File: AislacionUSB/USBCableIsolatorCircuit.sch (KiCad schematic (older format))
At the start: 54 parts, among them CON1 BARREL_JACK, J1 MICRO_USB, J2 IN_VCC, P1 USB_A, U1 PRTR5V0U2X, U2 ADUM5000, U3 7805, U4 PRTR5V0U2X

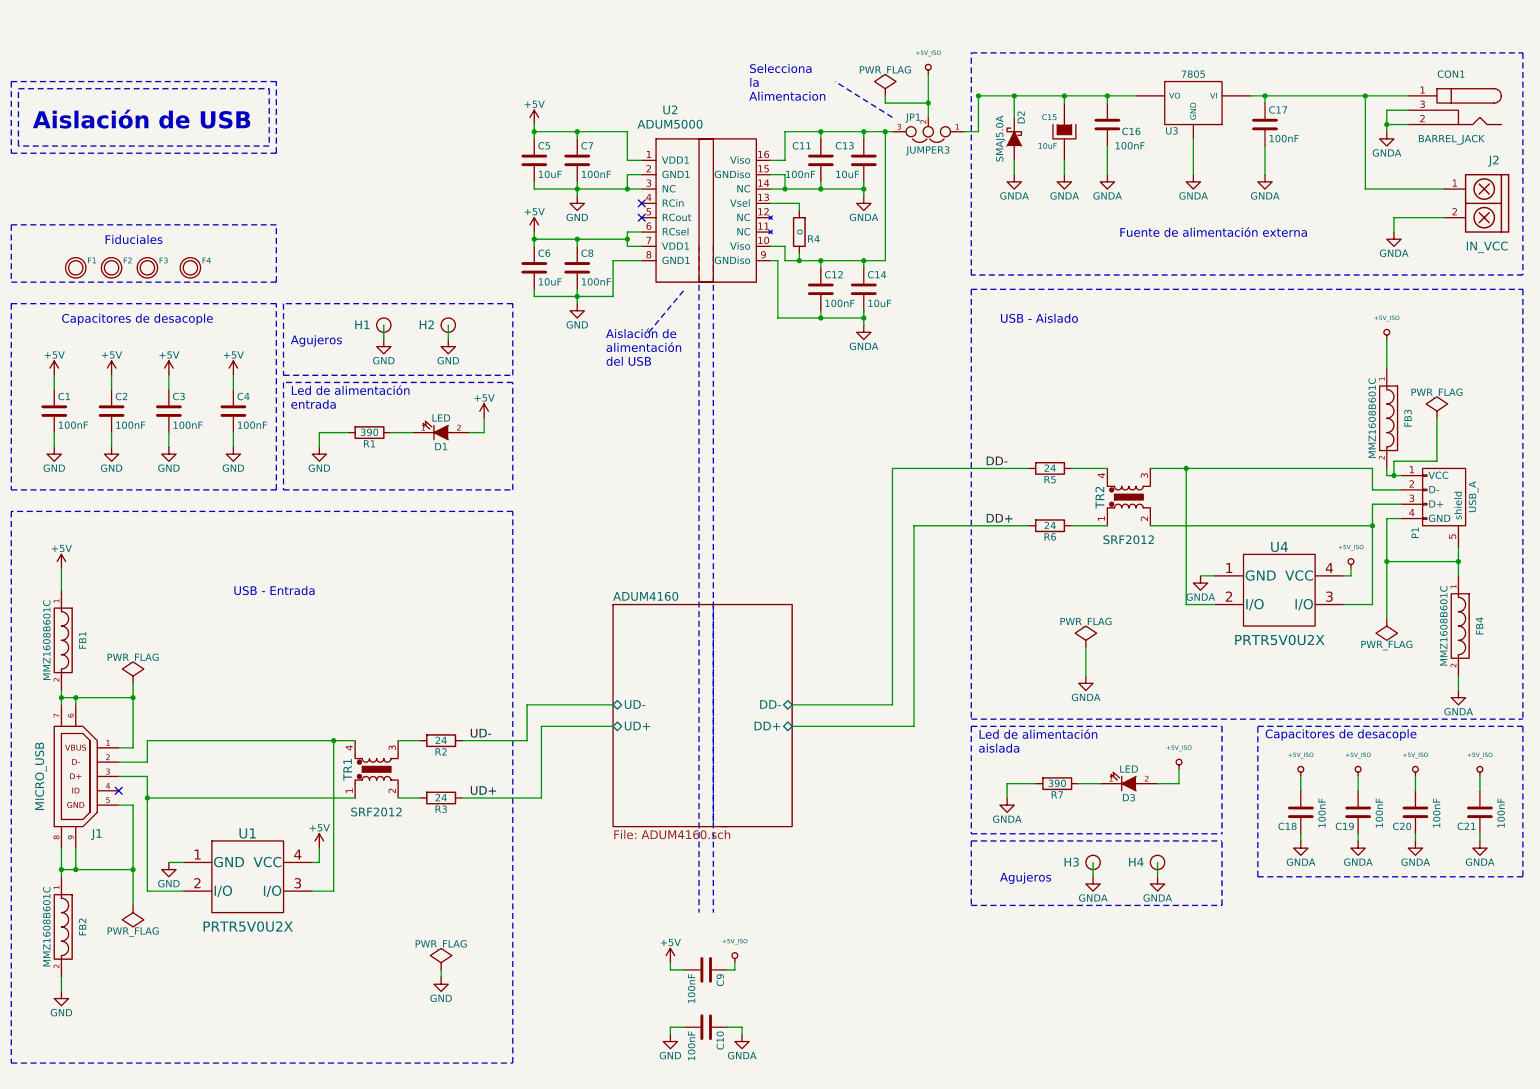
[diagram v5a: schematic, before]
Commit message: Primer ruteo - Se eliminaron los agujeros
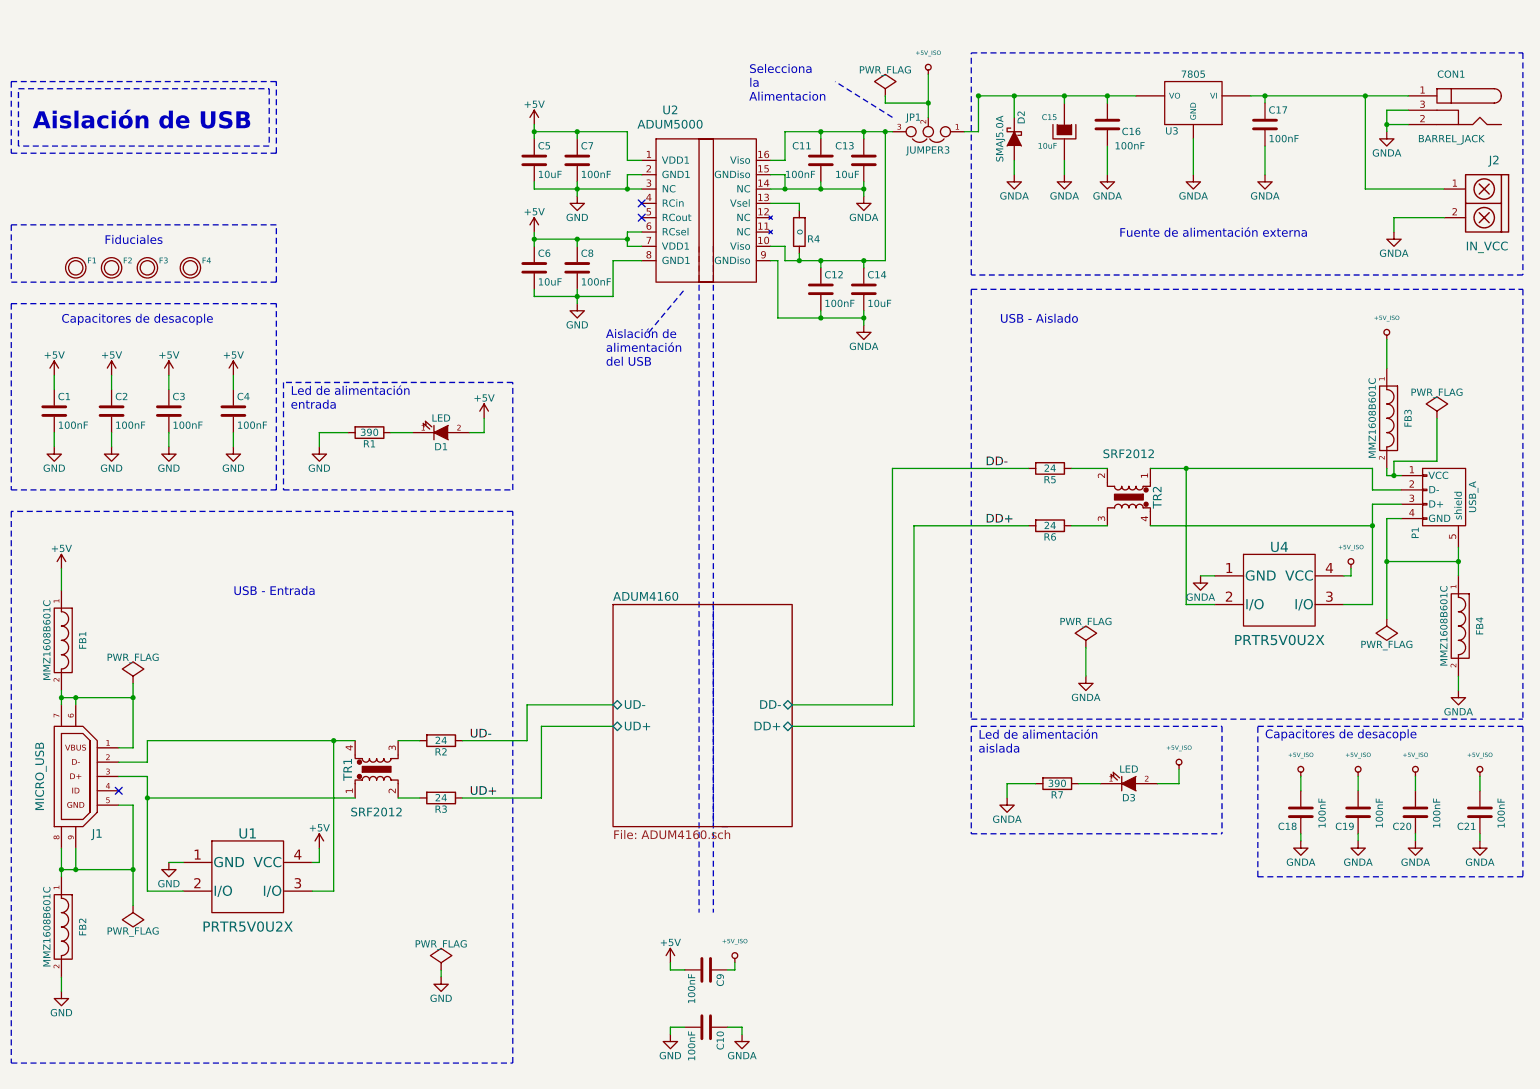
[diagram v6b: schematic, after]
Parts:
- removed H1, H2, H3, H4: PCB_HOLE, Mounting_Holes:MountingHole_2.7mm, symbol PCB_HOLE
- D2: footprint Diodes_SMD:DO-214AB_Handsoldering -> AislacionUSB:DO-214AC_SMA
- F1, F2, F3, F4: footprint Fiducials:Fiducial_1mm_Dia_2.54mm_Outer_CopperBottom -> AislacionUSB:Fiducial_1mm
- U3: Desc Linear Voltage Regulator IC Positive Fixed 1 Output 5V 1A TO-220AB -> Linear Voltage Regulator IC Positive Fixed 1 Output 5V 1A TO-220AB
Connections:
- net at P1.2 (D-), U4.2 (I/O): now also TR2.1; no longer TR2.3
- net at P1.3 (D+), U4.3 (I/O): now also TR2.4; no longer TR2.2
- net at R6.1: now also TR2.3; no longer TR2.1
- net at R5.1: now also TR2.2; no longer TR2.4
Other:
- note removed: "Agujeros"
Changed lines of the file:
@@
 $EndDescr
-$Comp
-L 7805 U3
-U 1 1 577C4B1F
-P 8850 900
-F 0 "U3" H 9000 704 50  0000 C CNN
-F 1 "7805" H 8850 1100 50  0000 C CNN
-F 2 "Power_Integrations:TO-220" H 8850 900 50  0001 C CNN
-F 3 "" H 8850 900 50  0000 C CNN
-F 4 "	Linear Voltage Regulator IC Positive Fixed 1 Output 5V 1A TO-220AB" H 8850 900 60  0001 C CNN "Desc"
-F 5 "LM7805CT-ND" H 8850 900 60  0001 C CNN "Digikey#"
-F 6 "LM7805CT" H 8850 900 60  0001 C CNN "Manf#"
-F 7 "Fairchild Semiconductor" H 8850 900 60  0001 C CNN "Manf"
-	1    8850 900
-	-1   0    0    -1
-$EndComp
 $Comp
 L BARREL_JACK CON1
@@
 F 0 "D2" H 7450 1100 50  0000 C CNN
 F 1 "SMAJ5.0A" H 7600 1250 50  0000 C CNN
-F 2 "Diodes_SMD:DO-214AB_Handsoldering" H 7600 1150 50  0001 C CNN
+F 2 "AislacionUSB:DO-214AC_SMA" H 7600 1150 50  0001 C CNN
 F 3 "" H 7600 1150 50  0000 C CNN
 F 4 "SMAJ5.0ABCT-ND" H 7600 1150 60  0001 C CNN "Digikey#"
@@
 F 0 "F1" H 1130 2100 40  0000 L CNN
 F 1 "FIDUCIAL" H 1050 1950 30  0001 C CNN
-F 2 "Fiducials:Fiducial_1mm_Dia_2.54mm_Outer_CopperBottom" H 1050 2100 60  0001 C CNN
+F 2 "AislacionUSB:Fiducial_1mm" H 1050 2100 60  0001 C CNN
 F 3 "" H 1050 2100 60  0001 C CNN
 F 4 "FIDUCIAL" H 1100 1850 60  0001 C CNN "Descripcion"
@@
 F 0 "F2" H 1380 2100 40  0000 L CNN
 F 1 "FIDUCIAL" H 1300 1950 30  0001 C CNN
-F 2 "Fiducials:Fiducial_1mm_Dia_2.54mm_Outer_CopperBottom" H 1300 2100 60  0001 C CNN
+F 2 "AislacionUSB:Fiducial_1mm" H 1300 2100 60  0001 C CNN
 F 3 "" H 1300 2100 60  0001 C CNN
 F 4 "FIDUCIAL" H 1350 1850 60  0001 C CNN "Descripcion"
@@
 F 0 "F3" H 1630 2100 40  0000 L CNN
 F 1 "FIDUCIAL" H 1550 1950 30  0001 C CNN
-F 2 "Fiducials:Fiducial_1mm_Dia_2.54mm_Outer_CopperBottom" H 1550 2100 60  0001 C CNN
+F 2 "AislacionUSB:Fiducial_1mm" H 1550 2100 60  0001 C CNN
 F 3 "" H 1550 2100 60  0001 C CNN
 F 4 "FIDUCIAL" H 1600 1850 60  0001 C CNN "Descripcion"
@@
 F 0 "F4" H 1930 2100 40  0000 L CNN
 F 1 "FIDUCIAL" H 1850 1950 30  0001 C CNN
-F 2 "Fiducials:Fiducial_1mm_Dia_2.54mm_Outer_CopperBottom" H 1850 2100 60  0001 C CNN
+F 2 "AislacionUSB:Fiducial_1mm" H 1850 2100 60  0001 C CNN
 F 3 "" H 1850 2100 60  0001 C CNN
 F 4 "FIDUCIAL" H 1900 1850 60  0001 C CNN "Descripcion"
@@
 Text Notes 750  1100 0    118  ~ 24
 Aislación de USB\n
-$Comp
-L PCB_HOLE H1
-U 1 1 578E72CD
-P 3200 2450
-F 0 "H1" H 3050 2450 60  0000 C CNN
-F 1 "PCB_HOLE" H 2900 2350 60  0001 C CNN
-F 2 "Mounting_Holes:MountingHole_2.7mm" H 3050 2500 60  0001 C CNN
-F 3 "PCB HOLE" H 3150 2600 60  0001 C CNN
-	1    3200 2450
-	1    0    0    -1
-$EndComp
-$Comp
-L PCB_HOLE H2
-U 1 1 578E7442
-P 3650 2450
-F 0 "H2" H 3500 2450 60  0000 C CNN
-F 1 "PCB_HOLE" H 3350 2350 60  0001 C CNN
-F 2 "Mounting_Holes:MountingHole_2.7mm" H 3500 2500 60  0001 C CNN
-F 3 "PCB HOLE" H 3600 2600 60  0001 C CNN
-	1    3650 2450
-	1    0    0    -1
-$EndComp
-$Comp
-L GND #PWR046
-U 1 1 578E8B5D
-P 3200 2550
-F 0 "#PWR046" H 3200 2300 50  0001 C CNN
-F 1 "GND" H 3200 2400 50  0000 C CNN
-F 2 "" H 3200 2550 50  0000 C CNN
-F 3 "" H 3200 2550 50  0000 C CNN
-	1    3200 2550
-	1    0    0    -1
-$EndComp
-$Comp
-L GND #PWR047
-U 1 1 578E8EB5
-P 3650 2550
-F 0 "#PWR047" H 3650 2300 50  0001 C CNN
-F 1 "GND" H 3650 2400 50  0000 C CNN
-F 2 "" H 3650 2550 50  0000 C CNN
-F 3 "" H 3650 2550 50  0000 C CNN
-	1    3650 2550
-	1    0    0    -1
-$EndComp
 Wire Wire Line
 	1450 5400 1350 5400
@@
 Wire Notes Line
 	600  1750 600  2150
-Wire Wire Line
-	3200 2450 3200 2550
-Wire Wire Line
-	3650 2450 3650 2550
-Wire Notes Line
-	2500 2800 4100 2800
-Wire Notes Line
-	4100 2800 4100 2300
-Wire Notes Line
-	4100 2300 2500 2300
-Wire Notes Line
-	2500 2300 2500 2800
-Text Notes 2550 2600 0    60   ~ 0
-Agujeros
-$Comp
-L PCB_HOLE H3
-U 1 1 578ED4CE
-P 8150 6200
-F 0 "H3" H 8000 6200 60  0000 C CNN
-F 1 "PCB_HOLE" H 7850 6100 60  0001 C CNN
-F 2 "Mounting_Holes:MountingHole_2.7mm" H 8000 6250 60  0001 C CNN
-F 3 "PCB HOLE" H 8100 6350 60  0001 C CNN
-	1    8150 6200
-	1    0    0    -1
-$EndComp
-$Comp
-L PCB_HOLE H4
-U 1 1 578ED4D4
-P 8600 6200
-F 0 "H4" H 8450 6200 60  0000 C CNN
-F 1 "PCB_HOLE" H 8300 6100 60  0001 C CNN
-F 2 "Mounting_Holes:MountingHole_2.7mm" H 8450 6250 60  0001 C CNN
-F 3 "PCB HOLE" H 8550 6350 60  0001 C CNN
-	1    8600 6200
-	1    0    0    -1
-$EndComp
-Wire Wire Line
-	8150 6200 8150 6300
-Wire Wire Line
-	8600 6200 8600 6300
-Wire Notes Line
-	7300 6050 9050 6050
-Text Notes 7500 6350 0    60   ~ 0
-Agujeros
-Wire Notes Line
-	7300 6050 7300 6500
-Wire Notes Line
-	7300 6500 9050 6500
-Wire Notes Line
-	9050 6500 9050 6050
-$Comp
-L GNDA #PWR048
-U 1 1 578EE057
-P 8150 6300
-F 0 "#PWR048" H 8150 6050 50  0001 C CNN
-F 1 "GNDA" H 8150 6150 50  0000 C CNN
-F 2 "" H 8150 6300 50  0000 C CNN
-F 3 "" H 8150 6300 50  0000 C CNN
-	1    8150 6300
-	1    0    0    -1
-$EndComp
-$Comp
-L GNDA #PWR049
-U 1 1 578EE1B1
-P 8600 6300
-F 0 "#PWR049" H 8600 6050 50  0001 C CNN
-F 1 "GNDA" H 8600 6150 50  0000 C CNN
-F 2 "" H 8600 6300 50  0000 C CNN
-F 3 "" H 8600 6300 50  0000 C CNN
-	1    8600 6300
-	1    0    0    -1
-$EndComp
 $Comp
 L C C10
@@
 F 7 "SRF2012-900Y" H 8400 3650 60  0001 C CNN "Manf#"
 	1    8400 3650
-	0    -1   -1   0
+	0    1    1    0
 $EndComp
 $Comp
@@
 NoConn ~ 1350 5700
 $Comp
-L PWR_FLAG #FLG050
+L PWR_FLAG #FLG046
 U 1 1 57901FA7
 P 1450 4950
-F 0 "#FLG050" H 1450 5045 50  0001 C CNN
+F 0 "#FLG046" H 1450 5045 50  0001 C CNN
 F 1 "PWR_FLAG" H 1450 5130 50  0000 C CNN
 F 2 "" H 1450 4950 50  0000 C CNN
@@
 $EndComp
 $Comp
-L PWR_FLAG #FLG051
+L PWR_FLAG #FLG047
 U 1 1 57902051
 P 1450 6500
-F 0 "#FLG051" H 1450 6595 50  0001 C CNN
+F 0 "#FLG047" H 1450 6595 50  0001 C CNN
 F 1 "PWR_FLAG" H 1450 6680 50  0000 C CNN
 F 2 "" H 1450 6500 50  0000 C CNN
@@
 Connection ~ 1450 6250
 $Comp
-L PWR_FLAG #FLG052
+L PWR_FLAG #FLG048
 U 1 1 579025E4
 P 10200 4500
-F 0 "#FLG052" H 10200 4595 50  0001 C CNN
+F 0 "#FLG048" H 10200 4595 50  0001 C CNN
 F 1 "PWR_FLAG" H 10200 4680 50  0000 C CNN
 F 2 "" H 10200 4500 50  0000 C CNN
@@
 Connection ~ 10200 4100
 $Comp
-L PWR_FLAG #FLG053
+L PWR_FLAG #FLG049
 U 1 1 5790310F
 P 10550 3100
-F 0 "#FLG053" H 10550 3195 50  0001 C CNN
+F 0 "#FLG049" H 10550 3195 50  0001 C CNN
 F 1 "PWR_FLAG" H 10550 3280 50  0000 C CNN
 F 2 "" H 10550 3100 50  0000 C CNN
@@
 Connection ~ 10250 3500
 $Comp
-L PWR_FLAG #FLG054
+L PWR_FLAG #FLG050
 U 1 1 57904563
 P 3600 6950
-F 0 "#FLG054" H 3600 7045 50  0001 C CNN
+F 0 "#FLG050" H 3600 7045 50  0001 C CNN
 F 1 "PWR_FLAG" H 3600 7130 50  0000 C CNN
 F 2 "" H 3600 6950 50  0000 C CNN
@@
 $EndSheet
 $Comp
-L PWR_FLAG #FLG055
+L PWR_FLAG #FLG051
 U 1 1 57907C7B
 P 6700 850
-F 0 "#FLG055" H 6700 945 50  0001 C CNN
+F 0 "#FLG051" H 6700 945 50  0001 C CNN
 F 1 "PWR_FLAG" H 6700 1030 50  0000 C CNN
 F 2 "" H 6700 850 50  0000 C CNN
@@
 	950  4150 950  4300
 $Comp
-L GND #PWR056
+L GND #PWR052
 U 1 1 5790C008
 P 3600 7000
-F 0 "#PWR056" H 3600 6750 50  0001 C CNN
+F 0 "#PWR052" H 3600 6750 50  0001 C CNN
 F 1 "GND" H 3600 6850 50  0000 C CNN
 F 2 "" H 3600 7000 50  0000 C CNN
@@
 Connection ~ 1450 5050
 $Comp
-L GNDA #PWR057
+L GNDA #PWR053
 U 1 1 5785B144
 P 10700 5000
-F 0 "#PWR057" H 10700 4750 50  0001 C CNN
+F 0 "#PWR053" H 10700 4750 50  0001 C CNN
 F 1 "GNDA" H 10700 4850 50  0000 C CNN
 F 2 "" H 10700 5000 50  0000 C CNN
@@
 $EndComp
 $Comp
-L GNDA #PWR058
+L GNDA #PWR054
 U 1 1 5790D610
 P 8100 4900
-F 0 "#PWR058" H 8100 4650 50  0001 C CNN
+F 0 "#PWR054" H 8100 4650 50  0001 C CNN
 F 1 "GNDA" H 8100 4750 50  0000 C CNN
 F 2 "" H 8100 4900 50  0000 C CNN
@@
 $EndComp
 $Comp
-L PWR_FLAG #FLG059
+L PWR_FLAG #FLG055
 U 1 1 5790D6D2
 P 8100 4700
-F 0 "#FLG059" H 8100 4795 50  0001 C CNN
+F 0 "#FLG055" H 8100 4795 50  0001 C CNN
 F 1 "PWR_FLAG" H 8100 4880 50  0000 C CNN
 F 2 "" H 8100 4700 50  0000 C CNN
@@
 Wire Notes Line
 	6750 1000 6350 750
+$Comp
+L 7805 U3
+U 1 1 57918B3E
+P 8850 900
+F 0 "U3" H 9000 704 50  0000 C CNN
+F 1 "7805" H 8850 1100 50  0000 C CNN
+F 2 "Power_Integrations:TO-220" H 8850 900 50  0001 C CNN
+F 3 "" H 8850 900 50  0000 C CNN
+F 4 "Linear Voltage Regulator IC Positive Fixed 1 Output 5V 1A TO-220AB" H 8850 900 60  0001 C CNN "Desc"
+F 5 "LM7805CT-ND" H 8850 900 60  0001 C CNN "Digikey#"
+F 6 "LM7805CT" H 8850 900 60  0001 C CNN "Manf#"
+F 7 "Fairchild Semiconductor" H 8850 900 60  0001 C CNN "Manf"
+	1    8850 900
+	-1   0    0    -1
+$EndComp
 $EndSCHEMATC

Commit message: Leyendas en el PCB
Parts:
- U3: symbol 7805 -> 7805-RESCUE-USBCableIsolatorCircuit
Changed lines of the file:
@@
 EESchema Schematic File Version 2
+LIBS:USBCableIsolatorCircuit-rescue
 LIBS:power
 LIBS:device
@@
 	6750 1000 6350 750
 $Comp
-L 7805 U3
+L 7805-RESCUE-USBCableIsolatorCircuit U3
 U 1 1 57918B3E
 P 8850 900

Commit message: Se agregaron cambios sugeridos por el docente - DOC:Sugerencias Docente 20160724
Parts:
- added H1, H2, H3: PCB_HOLE, AislacionUSB:MountingHole_2.7mm_M2.5_DIN965_Pad, symbol PCB_HOLE
- C1, C11, C12, C16, C17, C18, C19, C2, C20, C21, C3, C4, C7, C8, FB1, FB2, FB3, FB4: footprint Capacitors_SMD:C_0603_HandSoldering -> AislacionUSB:C_0603_HandSoldering
- C10, C9: footprint Capacitors_SMD:C_1812_HandSoldering -> AislacionUSB:C_1812_HandSoldering
- C13, C14, C5, C6: footprint Capacitors_SMD:C_1206_HandSoldering -> AislacionUSB:C_1206_HandSoldering
- C15: footprint SMD_Packages:SMD-1206_Pol -> AislacionUSB:SMD-1206_Pol
- CON1: footprint Connect:JACK_ALIM -> AislacionUSB:JACK_ALIM
- D1, D3: footprint LEDs:LED_0805 -> AislacionUSB:LED_0805
- J2: footprint Connect:bornier2 -> AislacionUSB:bornier2
- JP1: footprint Connect:PINHEAD1-3 -> AislacionUSB:PIN_ARRAY_3x1
- P1: footprint Connect:USB_A -> AislacionUSB:USB_A
- R1, R7: footprint Resistors_SMD:R_0805_HandSoldering -> AislacionUSB:R_0603_HandSoldering; Desc RES SMD 390 OHM 5% 1/8W 0805 -> RES SMD 390 OHM 5% 1/4W 0603; Digikey# P390ACT-ND -> P390BZCT-ND; Manf# ERJ-6GEYJ391V -> ERJ-PA3J391V
- R2, R3: footprint Resistors_SMD:R_0805_HandSoldering -> AislacionUSB:R_0603_HandSoldering
- R4, R5, R6: footprint Resistors_SMD:R_0603_HandSoldering -> AislacionUSB:R_0603_HandSoldering
- U2: footprint Housings_SOIC:SOIC-16_7.5x10.3mm_Pitch1.27mm -> AislacionUSB:ADUM5000
- U3: footprint Power_Integrations:TO-220 -> AislacionUSB:TO-220
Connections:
- net GND: now also H1.1
- net GNDA: now also H2.1, H3.1
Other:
- note added: "Agujeros"
